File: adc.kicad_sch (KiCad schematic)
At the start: 86 parts, among them J501 Screw_Terminal_01x02, J502 Screw_Terminal_01x02, J503 Screw_Terminal_01x02, J504 Screw_Terminal_01x02, J505 Screw_Terminal_01x02, J506 Screw_Terminal_01x02, U501 ADS131M08IRSNR, U502 TSV914AIDR, U503 TSV914AIDR, U504 TSV914AIDR

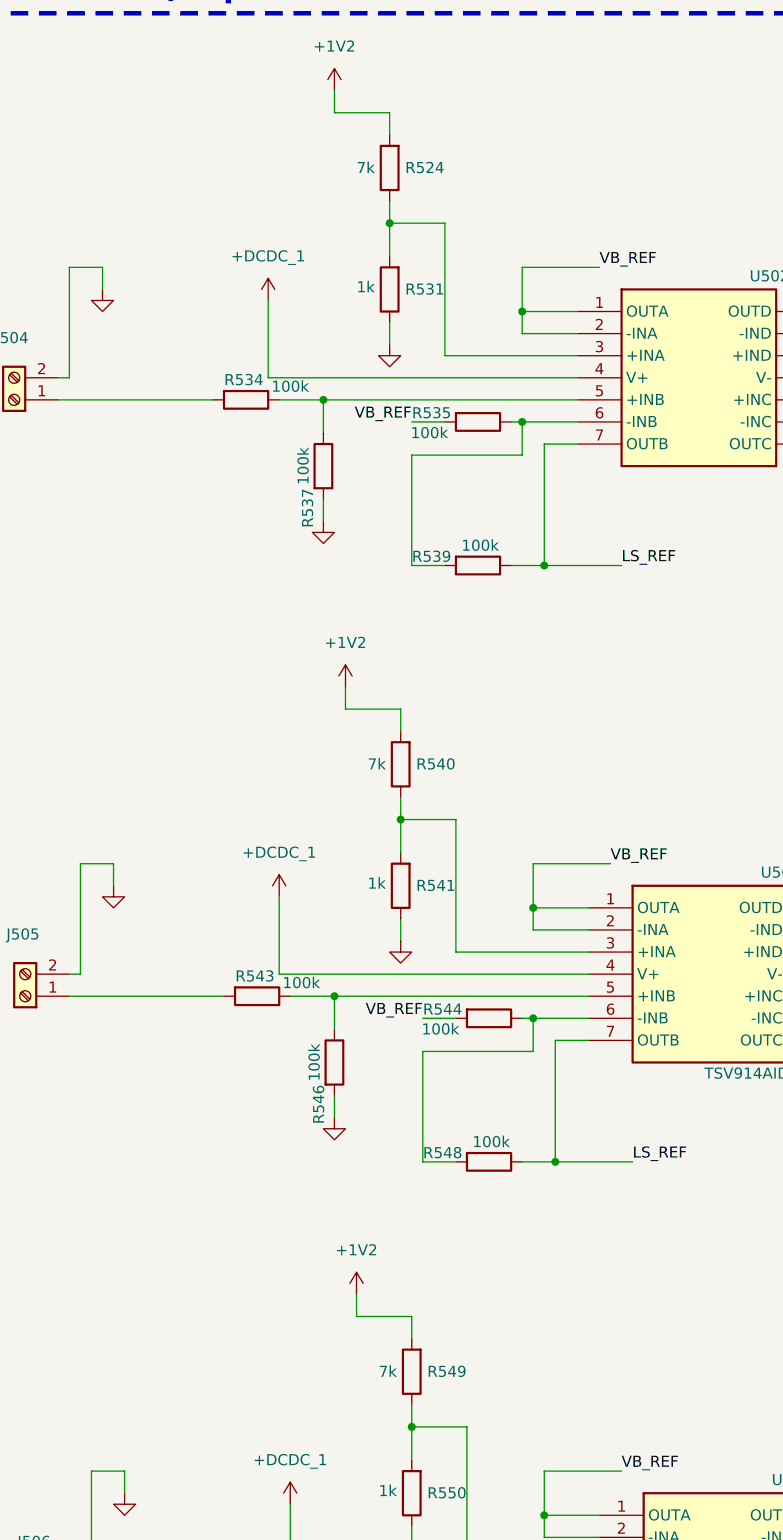
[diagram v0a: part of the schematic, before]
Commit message: components with distributor links added
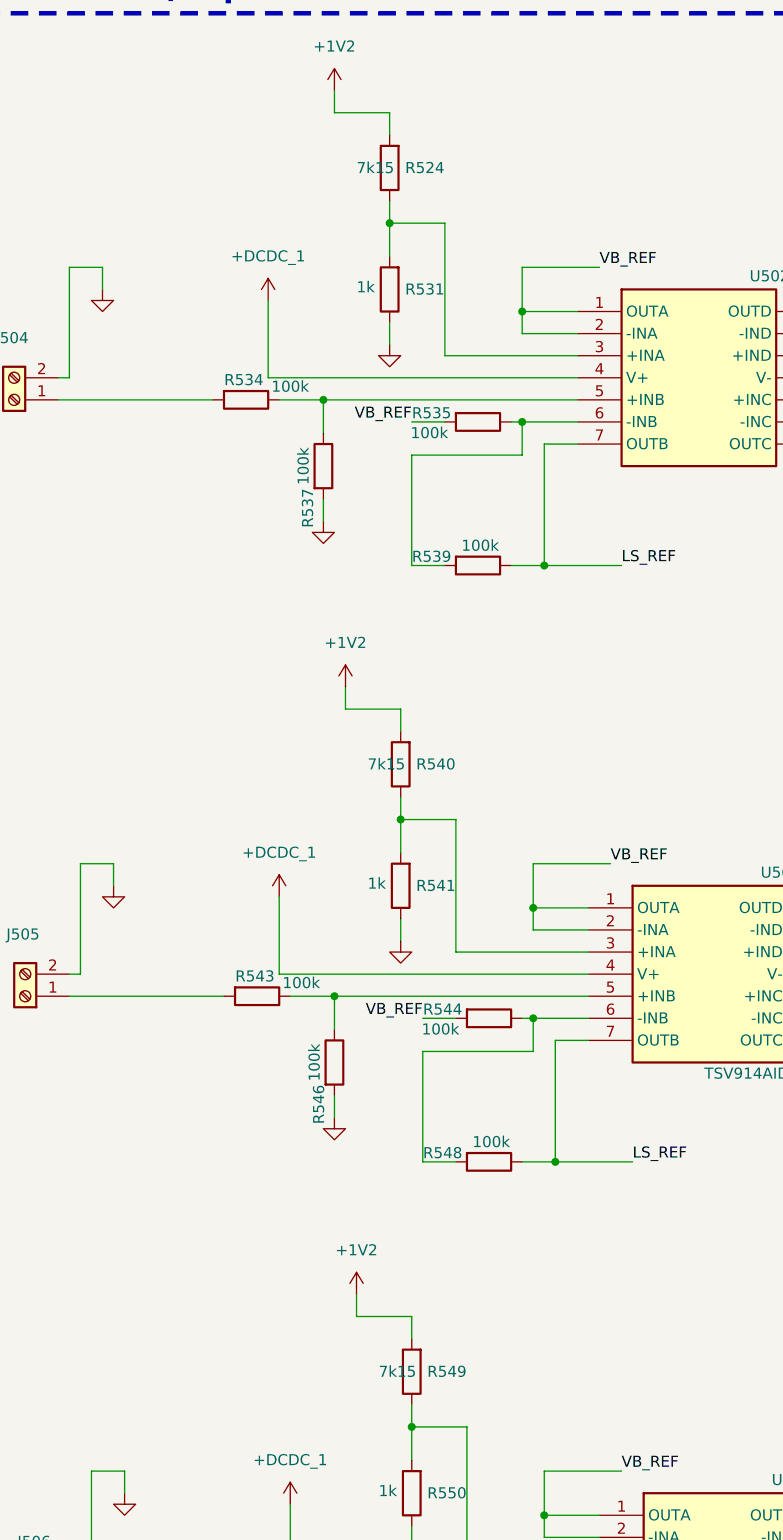
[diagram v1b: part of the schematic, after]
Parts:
- C501, C503, C504, C506, C507, C509, C513, C514, C516, C518: Distributor_Link (none) -> https://www.mouser.com/ProductDetail/Murata-Electronics/GCM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; Manufacturer_Name (none) -> Murata Electronics; Manufacturer_Part_Number (none) -> GCM1885C2A100JA16D
- C502, C505, C508, C515, C517, C519: Distributor_Link (none) -> https://www.mouser.com/ProductDetail/TDK/CGA3EANP02A682J080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; Manufacturer_Name (none) -> TDK; Manufacturer_Part_Number (none) -> CGA3EANP02A682J080AC
- C510: Distributor_Link (none) -> https://www.mouser.com/ProductDetail/TDK/CGA2B2X7R1C224K050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; Manufacturer_Name (none) -> TDK; Manufacturer_Part_Number (none) -> CGA2B2X7R1C224K050BE
- C511, C512: footprint Capacitor_SMD:C_0603_1608Metric -> Capacitor_SMD:C_0402_1005Metric; Distributor_Link (none) -> https://www.mouser.com/ProductDetail/KYOCERA-AVX/KGM05AR70J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; Manufacturer_Name (none) -> KYOCERA AVX; Manufacturer_Part_Number (none) -> KGM05AR70J105KH
- J501, J502, J503, J504, J505, J506: Distributor_Link (none) -> https://www.mouser.com/ProductDetail/Phoenix-Contact/154812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; Manufacturer_Name (none) -> Phoenix Contact; Manufacturer_Part_Number (none) -> 1548128
- R501, R502, R503, R508, R509, R510, R515, R516, R517: footprint Resistor_SMD:R_0603_1608Metric -> Resistor_SMD:R_0805_2012Metric; Distributor_Link (none) -> https://www.mouser.com/ProductDetail/Vishay-Dale/TNPV080533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; Manufacturer_Name (none) -> Vishay/Dale; Manufacturer_Part_Number (none) -> TNPV0805330KBEEA
- R504, R507, R511, R514, R518, R521, R531, R541, R550: Distributor_Link (none) -> https://www.mouser.com/ProductDetail/Vishay-Dale/CRCW06031K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; Manufacturer_Name (none) -> Vishay/Dale; Manufacturer_Part_Number (none) -> CRCW06031K00FKEE
- R505, R512, R519: Distributor_Link (none) -> https://www.mouser.com/ProductDetail/EPCOS-TDK/B72220S0271K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; Manufacturer_Name (none) -> EPCOS/TDK; Manufacturer_Part_Number (none) -> B72220S0271K101
- R506, R513, R520: footprint Resistor_SMD:R_0603_1608Metric -> Resistor_SMD:R_0805_2012Metric; Distributor_Link (none) -> https://www.mouser.com/ProductDetail/YAGEO/RT0805FRE10750RL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; Manufacturer_Name (none) -> YAGEO; Manufacturer_Part_Number (none) -> RT0805FRE10750RL
- R522, R523: Distributor_Link (none) -> https://www.mouser.com/ProductDetail/ROHM-Semiconductor/ESR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; Manufacturer_Name (none) -> ROHM Semiconductor; Manufacturer_Part_Number (none) -> ESR03EZPF33R0
- R524, R540, R549: value 7k -> 7k15; Distributor_Link (none) -> https://www.mouser.com/ProductDetail/KOA-Speer/RK73H1JTTDD7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; Manufacturer_Name (none) -> KOA Speer; Manufacturer_Part_Number (none) -> RK73H1JTTDD7151F
- R525, R527, R529, R533: footprint Resistor_SMD:R_0402_1005Metric -> Resistor_SMD:R_0603_1608Metric; Distributor_Link (none) -> https://www.mouser.com/ProductDetail/ROHM-Semiconductor/ESR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; Manufacturer_Name (none) -> ROHM Semiconductor; Manufacturer_Part_Number (none) -> ESR03EZPF33R0
- R526, R538, R547, R556: Distributor_Link (none) -> https://www.mouser.com/ProductDetail/Vishay-Dale/CRCW060310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; Manufacturer_Name (none) -> Vishay/Dale; Manufacturer_Part_Number (none) -> CRCW060310K0FKEI
- R528, R530, R534, R535, R537, R539, R543, R544, R546, R548, R552, R553, R555, R557: Distributor_Link (none) -> https://www.mouser.com/ProductDetail/Vishay-Dale/CRCW060310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; Manufacturer_Name (none) -> Vishay/Dale; Manufacturer_Part_Number (none) -> CRCW0603100KFKEE
- R532, R542, R551: Distributor_Link (none) -> https://www.mouser.com/ProductDetail/Panasonic/ERJ-PA3F2001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; Manufacturer_Name (none) -> Panasonic; Manufacturer_Part_Number (none) -> ERJ-PA3F2001V
- R536, R545, R554: Distributor_Link (none) -> https://www.mouser.com/ProductDetail/Panasonic/ERJ-H3EF6202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; Manufacturer_Name (none) -> Panasonic; Manufacturer_Part_Number (none) -> ERJ-H3EF6202V
- U501: Distributor_Link (none) -> https://www.mouser.com/ProductDetail/Texas-Instruments/ADS1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; Manufacturer_Name (none) -> Texas Instruments; Manufacturer_Part_Number (none) -> ADS131M08IRSNR
- U502, U503, U504: Distributor_Link (none) -> https://www.mouser.co.uk/ProductDetail/Texas-Instruments/TS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

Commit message: minor improvements to net labeling
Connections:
- net SPI1_SCK renamed ADS_SPI1_SCK
- net STM32_CLKOUT renamed ADS_STM32_CLKOUT
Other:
- note added: "For single-ended inputs, either AINxP and AINxN are connected to ground. Refer to the forum e2e.ti.com"
- note added: "LP Filter 11.7kHz"
- note added: "LP Filter 7.9MHz"
- note added: "Synchronous ADC"
- moved on the sheet: C510, C511, C512, C513, R522, R523, R525, R526, R527, R528, R529, R530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

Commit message: routed board power supply
1. USB
2. LDO for DCDC_1 and DCDC_2
3. LDO for +1V2
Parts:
- renumbered R524 to R523, R523 to R524, R531 to R527, R527 to R528, R528 to R529, R532 to R530, R529 to R531, R530 to R532, R534 to R533, R535 to R534, R533 to R535
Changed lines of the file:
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@@
 		(on_board yes)
 		(dnp no)
-		(property "Reference" "R524"
+		(property "Reference" "R523"
 			(at 74.168 182.88 0)
 			(effects
@@
 			(project "EnergyMonitoringSystem"
 				(path "/e660428c-c9b7-476c-8ac8-2d419f233469/817d89b0-4ccf-433f-9d8b-ff122ae0551e"
-					(reference "R524")
+					(reference "R523")
 					(unit 1)
 				)
@@
 		(dnp no)
 		(fields_autoplaced yes)
-		(property "Reference" "#PWR0526"
+		(property "Reference" "#PWR0525"
 			(at 73.66 248.158 0)
 			(effects
@@
 			(project "EnergyMonitoringSystem"
 				(path "/e660428c-c9b7-476c-8ac8-2d419f233469/817d89b0-4ccf-433f-9d8b-ff122ae0551e"
-					(reference "#PWR0526")
+					(reference "#PWR0525")
 					(unit 1)
 				)
@@
 		(dnp no)
 		(fields_autoplaced yes)
-		(property "Reference" "#PWR0522"
+		(property "Reference" "#PWR0521"
 			(at 212.09 227.33 0)
 			(effects
@@
 			(project "EnergyMonitoringSystem"
 				(path "/e660428c-c9b7-476c-8ac8-2d419f233469/817d89b0-4ccf-433f-9d8b-ff122ae0551e"
-					(reference "#PWR0522")
+					(reference "#PWR0521")
 					(unit 1)
 				)
@@
 		(dnp no)
 		(fields_autoplaced yes)
-		(property "Reference" "#PWR0507"
+		(property "Reference" "#PWR0506"
 			(at 96.52 153.67 0)
 			(effects
@@
 			(project "EnergyMonitoringSystem"
 				(path "/e660428c-c9b7-476c-8ac8-2d419f233469/817d89b0-4ccf-433f-9d8b-ff122ae0551e"
-					(reference "#PWR0507")
+					(reference "#PWR0506")
 					(unit 1)
 				)
@@
 		(on_board yes)
 		(dnp no)
-		(property "Reference" "R534"
+		(property "Reference" "R533"
 			(at 55.626 207.264 90)
 			(effects
@@
 			(project "EnergyMonitoringSystem"
 				(path "/e660428c-c9b7-476c-8ac8-2d419f233469/817d89b0-4ccf-433f-9d8b-ff122ae0551e"
-					(reference "R534")
+					(reference "R533")
 					(unit 1)
 				)
@@
 		(dnp no)
 		(fields_autoplaced yes)
-		(property "Reference" "#PWR0525"
+		(property "Reference" "#PWR0526"
 			(at 415.29 248.92 0)
 			(effects
@@
 			(project "EnergyMonitoringSystem"
 				(path "/e660428c-c9b7-476c-8ac8-2d419f233469/817d89b0-4ccf-433f-9d8b-ff122ae0551e"
-					(reference "#PWR0525")
+					(reference "#PWR0526")
 					(unit 1)
 				)
@@
 		(on_board yes)
 		(dnp no)
-		(property "Reference" "R535"
+		(property "Reference" "R534"
 			(at 77.216 211.074 90)
 			(effects
@@
 			(project "EnergyMonitoringSystem"
 				(path "/e660428c-c9b7-476c-8ac8-2d419f233469/817d89b0-4ccf-433f-9d8b-ff122ae0551e"
-					(reference "R535")
+					(reference "R534")
 					(unit 1)
 				)
@@
 		(on_board yes)
 		(dnp no)
-		(property "Reference" "R523"
+		(property "Reference" "R524"
 			(at 422.656 185.166 90)
 			(effects
@@
 			(project "EnergyMonitoringSystem"
 				(path "/e660428c-c9b7-476c-8ac8-2d419f233469/817d89b0-4ccf-433f-9d8b-ff122ae0551e"
-					(reference "R523")
+					(reference "R524")
 					(unit 1)
 				)
@@
 		(dnp no)
 		(fields_autoplaced yes)
-		(property "Reference" "#PWR0523"
+		(property "Reference" "#PWR0522"
 			(at 64.77 229.87 0)
 			(effects
@@
 			(project "EnergyMonitoringSystem"
 				(path "/e660428c-c9b7-476c-8ac8-2d419f233469/817d89b0-4ccf-433f-9d8b-ff122ae0551e"
-					(reference "#PWR0523")
+					(reference "#PWR0522")
 					(unit 1)
 				)
@@
 		(dnp no)
 		(fields_autoplaced yes)
-		(property "Reference" "#PWR0506"
+		(property "Reference" "#PWR0507"
 			(at 353.314 144.78 0)
 			(effects
@@
 			(project "EnergyMonitoringSystem"
 				(path "/e660428c-c9b7-476c-8ac8-2d419f233469/817d89b0-4ccf-433f-9d8b-ff122ae0551e"
-					(reference "#PWR0506")
+					(reference "#PWR0507")
 					(unit 1)
 				)
@@
 		(on_board yes)
 		(dnp no)
-		(property "Reference" "R528"
+		(property "Reference" "R529"
 			(at 498.348 196.85 0)
 			(effects
@@
 			(project "EnergyMonitoringSystem"
 				(path "/e660428c-c9b7-476c-8ac8-2d419f233469/817d89b0-4ccf-433f-9d8b-ff122ae0551e"
-					(reference "R528")
+					(reference "R529")
 					(unit 1)
 				)
@@
 		(on_board yes)
 		(dnp no)
-		(property "Reference" "R533"
+		(property "Reference" "R535"
 			(at 428.498 209.042 90)
 			(effects
@@
 			(project "EnergyMonitoringSystem"
 				(path "/e660428c-c9b7-476c-8ac8-2d419f233469/817d89b0-4ccf-433f-9d8b-ff122ae0551e"
-					(reference "R533")
+					(reference "R535")
 					(unit 1)
 				)
@@
 		(on_board yes)
 		(dnp no)
-		(property "Reference" "R532"
+		(property "Reference" "R530"
 			(at 180.086 199.39 90)
 			(effects
@@
 			(project "EnergyMonitoringSystem"
 				(path "/e660428c-c9b7-476c-8ac8-2d419f233469/817d89b0-4ccf-433f-9d8b-ff122ae0551e"
-					(reference "R532")
+					(reference "R530")
 					(unit 1)
 				)
@@
 		(dnp no)
 		(fields_autoplaced yes)
-		(property "Reference" "#PWR0524"
+		(property "Reference" "#PWR0523"
 			(at 140.97 232.41 0)
 			(effects
@@
 			(project "EnergyMonitoringSystem"
 				(path "/e660428c-c9b7-476c-8ac8-2d419f233469/817d89b0-4ccf-433f-9d8b-ff122ae0551e"
-					(reference "#PWR0524")
+					(reference "#PWR0523")
 					(unit 1)
 				)
@@
 		(dnp no)
 		(fields_autoplaced yes)
-		(property "Reference" "#PWR0521"
+		(property "Reference" "#PWR0520"
 			(at 194.31 227.33 0)
 			(effects
@@
 			(project "EnergyMonitoringSystem"
 				(path "/e660428c-c9b7-476c-8ac8-2d419f233469/817d89b0-4ccf-433f-9d8b-ff122ae0551e"
-					(reference "#PWR0521")
+					(reference "#PWR0520")
 					(unit 1)
 				)
@@
 		(on_board yes)
 		(dnp no)
-		(property "Reference" "R527"
+		(property "Reference" "R528"
 			(at 422.656 195.326 90)
 			(effects
@@
 			(project "EnergyMonitoringSystem"
 				(path "/e660428c-c9b7-476c-8ac8-2d419f233469/817d89b0-4ccf-433f-9d8b-ff122ae0551e"
-					(reference "R527")
+					(reference "R528")
 					(unit 1)
 				)
@@
 		(on_board yes)
 		(dnp no)
-		(property "Reference" "R531"
+		(property "Reference" "R527"
 			(at 74.168 196.85 0)
 			(effects
@@
 			(project "EnergyMonitoringSystem"
 				(path "/e660428c-c9b7-476c-8ac8-2d419f233469/817d89b0-4ccf-433f-9d8b-ff122ae0551e"
-					(reference "R531")
+					(reference "R527")
 					(unit 1)
 				)
@@
 		(dnp no)
 		(fields_autoplaced yes)
-		(property "Reference" "#PWR0520"
+		(property "Reference" "#PWR0524"
 			(at 351.79 232.918 0)
 			(effects
@@
 			(project "EnergyMonitoringSystem"
 				(path "/e660428c-c9b7-476c-8ac8-2d419f233469/817d89b0-4ccf-433f-9d8b-ff122ae0551e"
-					(reference "#PWR0520")
+					(reference "#PWR0524")
 					(unit 1)
 				)
@@
 		(on_board yes)
 		(dnp no)
-		(property "Reference" "R529"
+		(property "Reference" "R531"
 			(at 422.656 200.406 90)
 			(effects
@@
 			(project "EnergyMonitoringSystem"
 				(path "/e660428c-c9b7-476c-8ac8-2d419f233469/817d89b0-4ccf-433f-9d8b-ff122ae0551e"
-					(reference "R529")
+					(reference "R531")
 					(unit 1)
 				)
@@
 		(on_board yes)
 		(dnp no)
-		(property "Reference" "R530"
+		(property "Reference" "R532"
 			(at 518.668 201.93 0)
 			(effects
@@
 			(project "EnergyMonitoringSystem"
 				(path "/e660428c-c9b7-476c-8ac8-2d419f233469/817d89b0-4ccf-433f-9d8b-ff122ae0551e"
-					(reference "R530")
+					(reference "R532")
 					(unit 1)
 				)
